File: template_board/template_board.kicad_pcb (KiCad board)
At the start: 4 copper layers, 90.2 x 95.9 mm, 131 parts, among them J1 USB_C_Receptacle_USB2.0_16P, J2 Conn_Coaxial, M1 MountingHole, M3 MountingHole, Q2 S9013, Q3 AO3400A, SW1 SW_Push, SW3 SW_Push, U1 IP4220CZ6, U11 FSUSB42UMX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

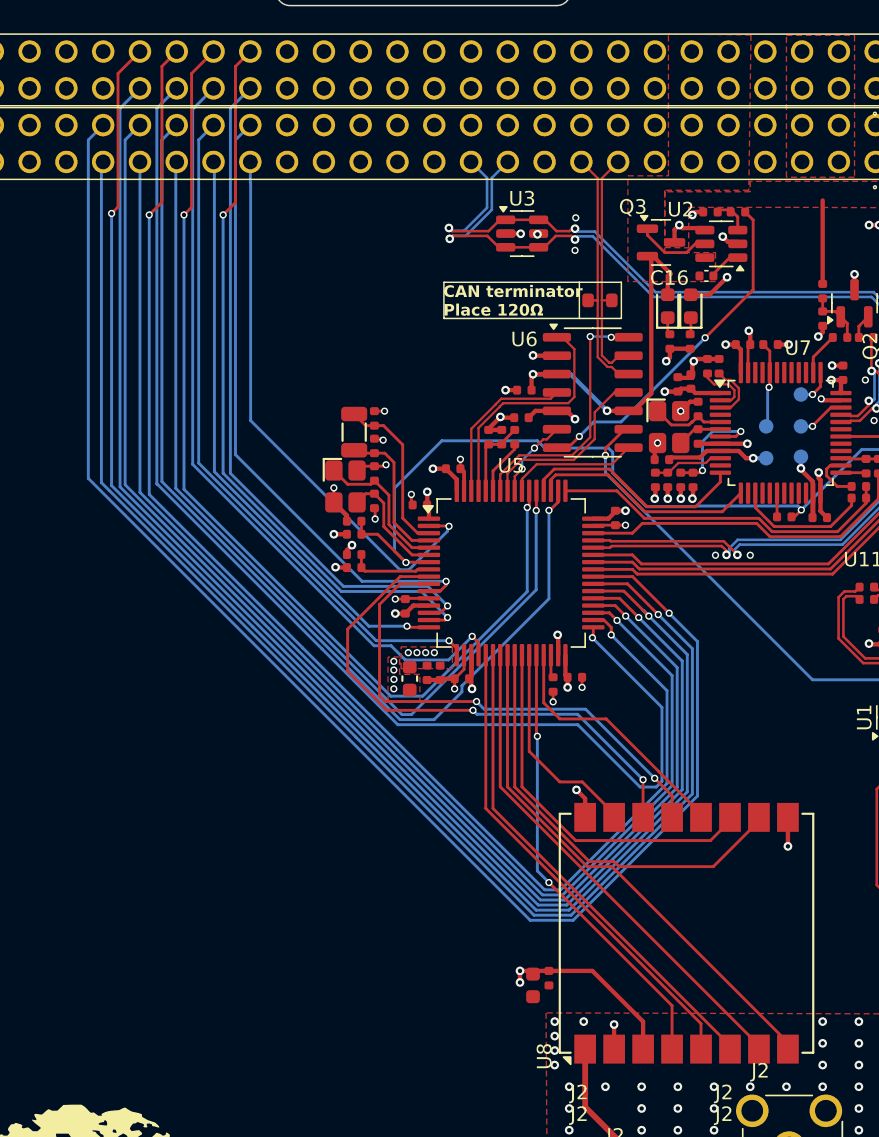
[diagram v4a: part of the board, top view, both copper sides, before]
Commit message: fixed SPI leyoud, added length matching
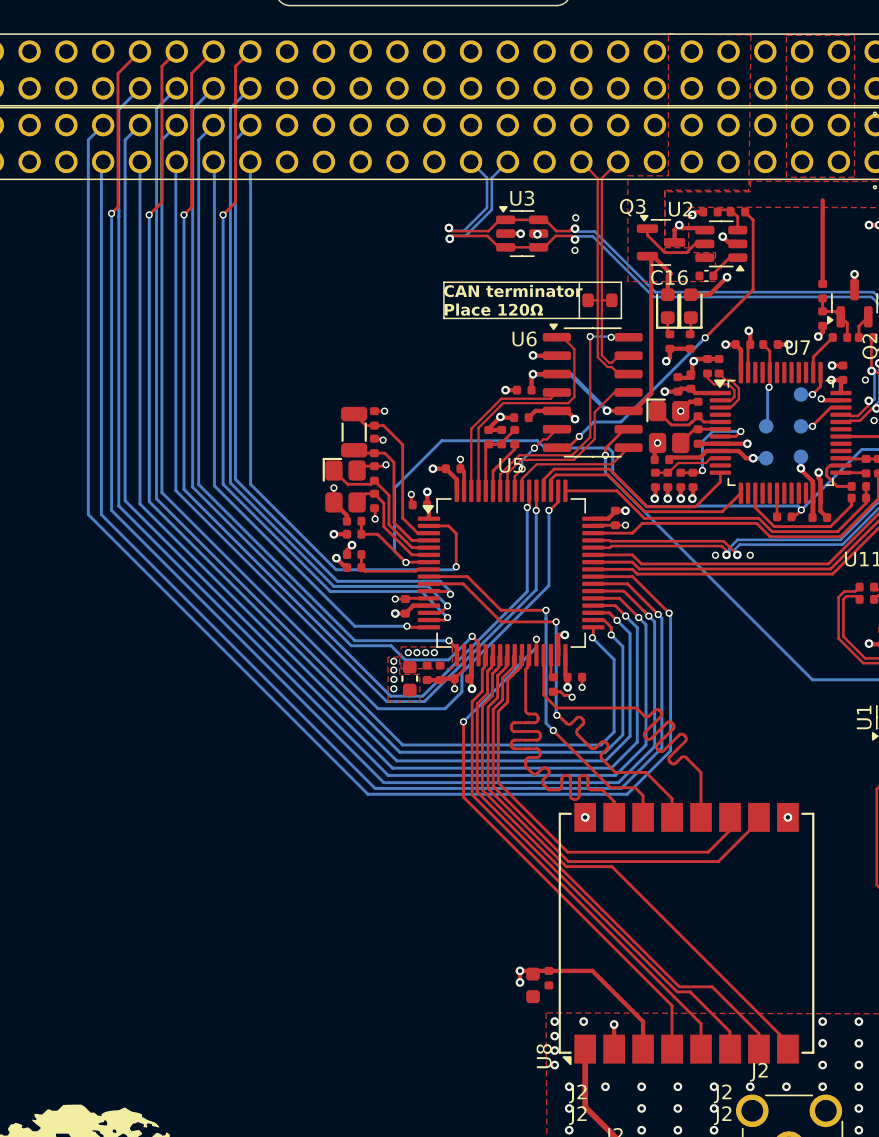
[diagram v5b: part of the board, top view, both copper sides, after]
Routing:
- net /LORA/LORA.CS: track 14.5 -> 30.2 mm
- net /BUS_CONNECTOR/GPIO26: track 95.3 -> 81.4 mm
- net /BUS_CONNECTOR/GPIO3: track 89.0 -> 75.7 mm
- net /BUS_CONNECTOR/GPIO11: track 94.3 -> 81.7 mm
- net /BUS_CONNECTOR/GPIO19: track 99.0 -> 87.1 mm
- net /LORA/LORA.CLK: track 17.6 -> 29.3 mm
- net /BUS_CONNECTOR/GPIO27: track 105.0 -> 93.7 mm
- net /BUS_CONNECTOR/GPIO4: track 97.6 -> 86.8 mm
- net /BUS_CONNECTOR/GPIO12: track 102.8 -> 92.6 mm
- net /LORA/LORA.MOSI: track 36.1 -> 27.1 mm
- net /BUS_CONNECTOR/GPIO18: track 84.3 -> 75.8 mm
- net /LORA/~{LORA_RESET}: track 31.1 -> 37.5 mm
- net /BUS_CONNECTOR/GPIO0: track 38.6 -> 43.4 mm
- net /LORA/LORA.MISO: track 34.9 -> 31.2 mm
- net /LORA/LORA_DIO5: track 26.0 -> 29.2 mm
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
